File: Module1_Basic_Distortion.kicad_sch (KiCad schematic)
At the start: 16 parts, among them J1 Conn_01x06_Socket, U1 TL071

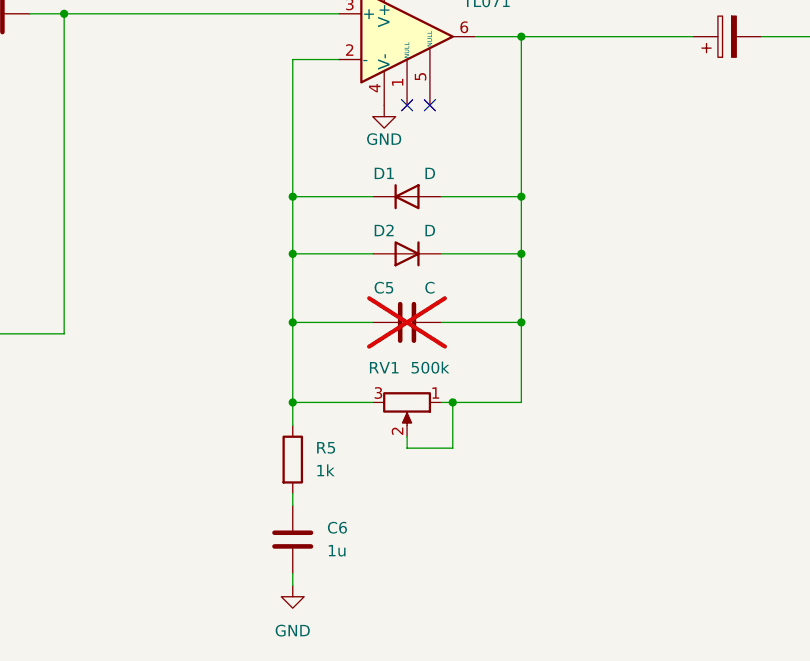
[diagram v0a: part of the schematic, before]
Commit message: Added footprints
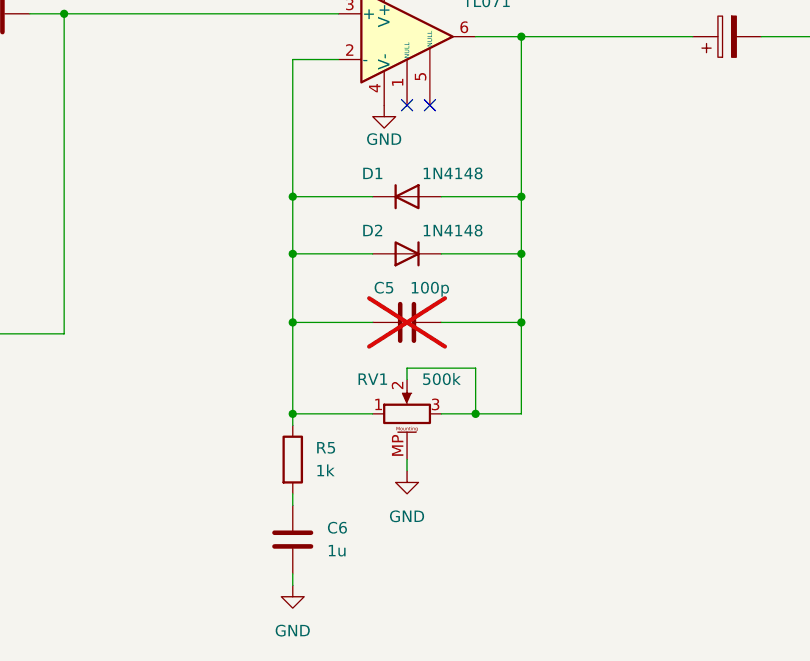
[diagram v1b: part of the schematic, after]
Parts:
- removed RV1: 500k, symbol Device:R_Potentiometer
- added RV1: 500k, Module1_Basic_Distortion:PBourns_TV09_Horizontal_RearMount, symbol Device:R_Potentiometer_MountingPin
- C1, C3, C4: footprint (none) -> Capacitor_THT:CP_Radial_D5.0mm_P2.00mm
- C2, C6: footprint (none) -> Capacitor_THT:C_Rect_L7.2mm_W5.5mm_P5.00mm_FKS2_FKP2_MKS2_MKP2
- C5: value C -> 100p; footprint (none) -> Capacitor_THT:C_Rect_L7.2mm_W5.5mm_P5.00mm_FKS2_FKP2_MKS2_MKP2
- D1, D2: value D -> 1N4148; footprint (none) -> Diode_THT:D_A-405_P10.16mm_Horizontal
- R1, R2, R3, R4, R5: footprint (none) -> Resistor_THT:R_Axial_DIN0309_L9.0mm_D3.2mm_P12.70mm_Horizontal
- U1: footprint (none) -> Package_DIP:DIP-8_W7.62mm_LongPads
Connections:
- net GND: now also RV1.MP (MountPin)
- net at C5.1, D1.1 (K), D2.2 (A)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: now also RV1.1
- net at C4.1, C5.2, D1.2 (A)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: now also RV1.2, RV1.3
